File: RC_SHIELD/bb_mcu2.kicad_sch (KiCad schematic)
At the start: 14 parts, among them J26 SWD, J27 P3a, SW1 SW_Push, U25 STM32F030K6Tx, Y1 8MHz

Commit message: footprints assigned
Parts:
- C10, C11, C12, C13, C14, C15, C16, C9: footprint (none) -> Capacitor_SMD:C_0805_2012Metric_Pad1.18x1.45mm_HandSolder
- J26: footprint (none) -> Connector_PinHeader_2.54mm:PinHeader_1x05_P2.54mm_Vertical_SMD_Pin1Left
- J27: footprint (none) -> Connector_Dsub:DSUB-37_Female_Horizontal_P2.77x2.84mm_EdgePinOffset7.70mm_Housed_MountingHolesOffset9.12mm
- R35: footprint (none) -> Resistor_SMD:R_0805_2012Metric_Pad1.20x1.40mm_HandSolder
- SW1: footprint (none) -> Button_Switch_SMD:SW_Tactile_SPST_NO_Straight_CK_PTS636Sx25SMTRLFS
- Y1: footprint (none) -> Crystal:Crystal_SMD_3225-4Pin_3.2x2.5mm_HandSoldering
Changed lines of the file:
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@@
       (effects (font (size 1.27 1.27)))
     )
-    (property "Footprint" "" (at 93.345 32.6898 0)
+    (property "Footprint" "Capacitor_SMD:C_0805_2012Metric_Pad1.18x1.45mm_HandSolder" (at 93.345 32.6898 0)
       (effects (font (size 1.27 1.27)) hide)
     )
@@
       (effects (font (size 1.27 1.27)))
     )
-    (property "Footprint" "" (at 74.295 22.5298 0)
+    (property "Footprint" "Capacitor_SMD:C_0805_2012Metric_Pad1.18x1.45mm_HandSolder" (at 74.295 22.5298 0)
       (effects (font (size 1.27 1.27)) hide)
     )
@@
       (effects (font (size 1.27 1.27)))
     )
-    (property "Footprint" "" (at 29.845 47.2948 0)
+    (property "Footprint" "Capacitor_SMD:C_0805_2012Metric_Pad1.18x1.45mm_HandSolder" (at 29.845 47.2948 0)
       (effects (font (size 1.27 1.27)) hide)
     )
@@
       (effects (font (size 1.27 1.27)))
     )
-    (property "Footprint" "" (at 35.56 53.975 0)
+    (property "Footprint" "Crystal:Crystal_SMD_3225-4Pin_3.2x2.5mm_HandSoldering" (at 35.56 53.975 0)
       (effects (font (size 1.27 1.27)) hide)
     )
@@
       (effects (font (size 1.27 1.27)))
     )
-    (property "Footprint" "" (at 74.295 32.6898 0)
+    (property "Footprint" "Capacitor_SMD:C_0805_2012Metric_Pad1.18x1.45mm_HandSolder" (at 74.295 32.6898 0)
       (effects (font (size 1.27 1.27)) hide)
     )
@@
       (effects (font (size 1.27 1.27)))
     )
-    (property "Footprint" "" (at 47.625 33.9598 0)
+    (property "Footprint" "Capacitor_SMD:C_0805_2012Metric_Pad1.18x1.45mm_HandSolder" (at 47.625 33.9598 0)
       (effects (font (size 1.27 1.27)) hide)
     )
@@
       (effects (font (size 1.27 1.27)))
     )
-    (property "Footprint" "" (at 93.345 22.5298 0)
+    (property "Footprint" "Capacitor_SMD:C_0805_2012Metric_Pad1.18x1.45mm_HandSolder" (at 93.345 22.5298 0)
       (effects (font (size 1.27 1.27)) hide)
     )
@@
       (effects (font (size 1.27 1.27)) (justify left))
     )
-    (property "Footprint" "" (at 56.2102 30.48 0)
+    (property "Footprint" "Capacitor_SMD:C_0805_2012Metric_Pad1.18x1.45mm_HandSolder" (at 56.2102 30.48 0)
       (effects (font (size 1.27 1.27)) hide)
     )
@@
       (effects (font (size 1.27 1.27)))
     )
-    (property "Footprint" "" (at 29.845 58.7248 0)
+    (property "Footprint" "Capacitor_SMD:C_0805_2012Metric_Pad1.18x1.45mm_HandSolder" (at 29.845 58.7248 0)
       (effects (font (size 1.27 1.27)) hide)
     )
@@
       (effects (font (size 1.27 1.27)))
     )
-    (property "Footprint" "" (at 43.815 21.59 0)
+    (property "Footprint" "Button_Switch_SMD:SW_Tactile_SPST_NO_Straight_CK_PTS636Sx25SMTRLFS" (at 43.815 21.59 0)
       (effects (font (size 1.27 1.27)) hide)
     )
@@
       (effects (font (size 1.27 1.27)) (justify left))
     )
-    (property "Footprint" "" (at 254 80.01 0)
+    (property "Footprint" "Connector_Dsub:DSUB-37_Female_Horizontal_P2.77x2.84mm_EdgePinOffset7.70mm_Housed_MountingHolesOffset9.12mm" (at 254 80.01 0)
       (effects (font (size 1.27 1.27)) hide)
     )
@@
       (effects (font (size 1.27 1.27)))
     )
-    (property "Footprint" "" (at 48.26 61.468 90)
+    (property "Footprint" "Resistor_SMD:R_0805_2012Metric_Pad1.20x1.40mm_HandSolder" (at 48.26 61.468 90)
       (effects (font (size 1.27 1.27)) hide)
     )
@@
       (effects (font (size 1.27 1.27)) (justify left))
     )
-    (property "Footprint" "" (at 139.065 85.09 0)
-      (effects (font (size 1.27 1.27)) hide)
-    )
+    (property "Footprint" "Connector_PinHeader_2.54mm:PinHeader_1x05_P2.54mm_Vertical_SMD_Pin1Left" (at 139.065 85.09 0)
+      (effects (font (size 1.27 1.27)) hide)
+    )

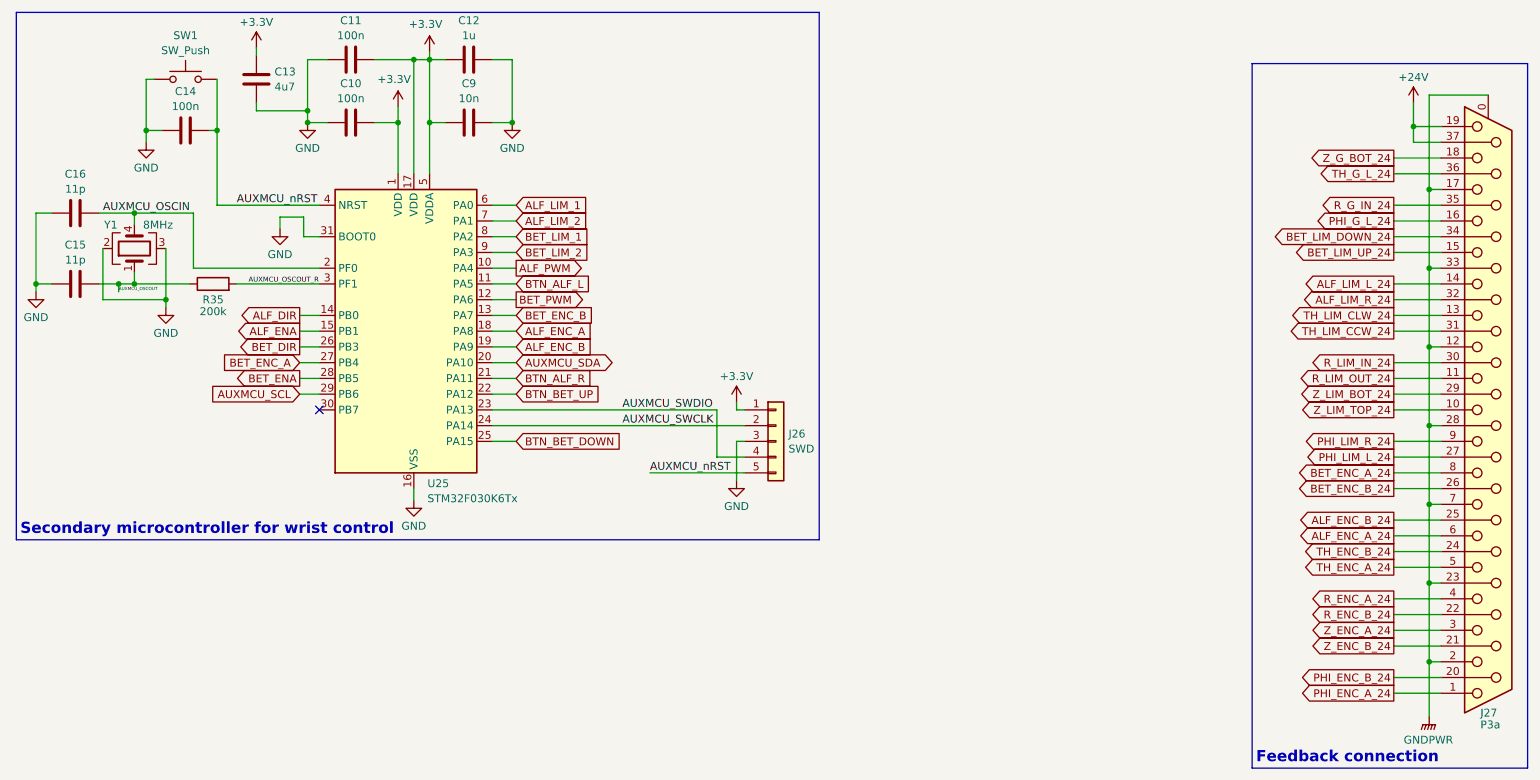
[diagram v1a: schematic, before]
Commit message: Fixed typos and names in schematic, changed optocoupler resistors; added .gitgnore file
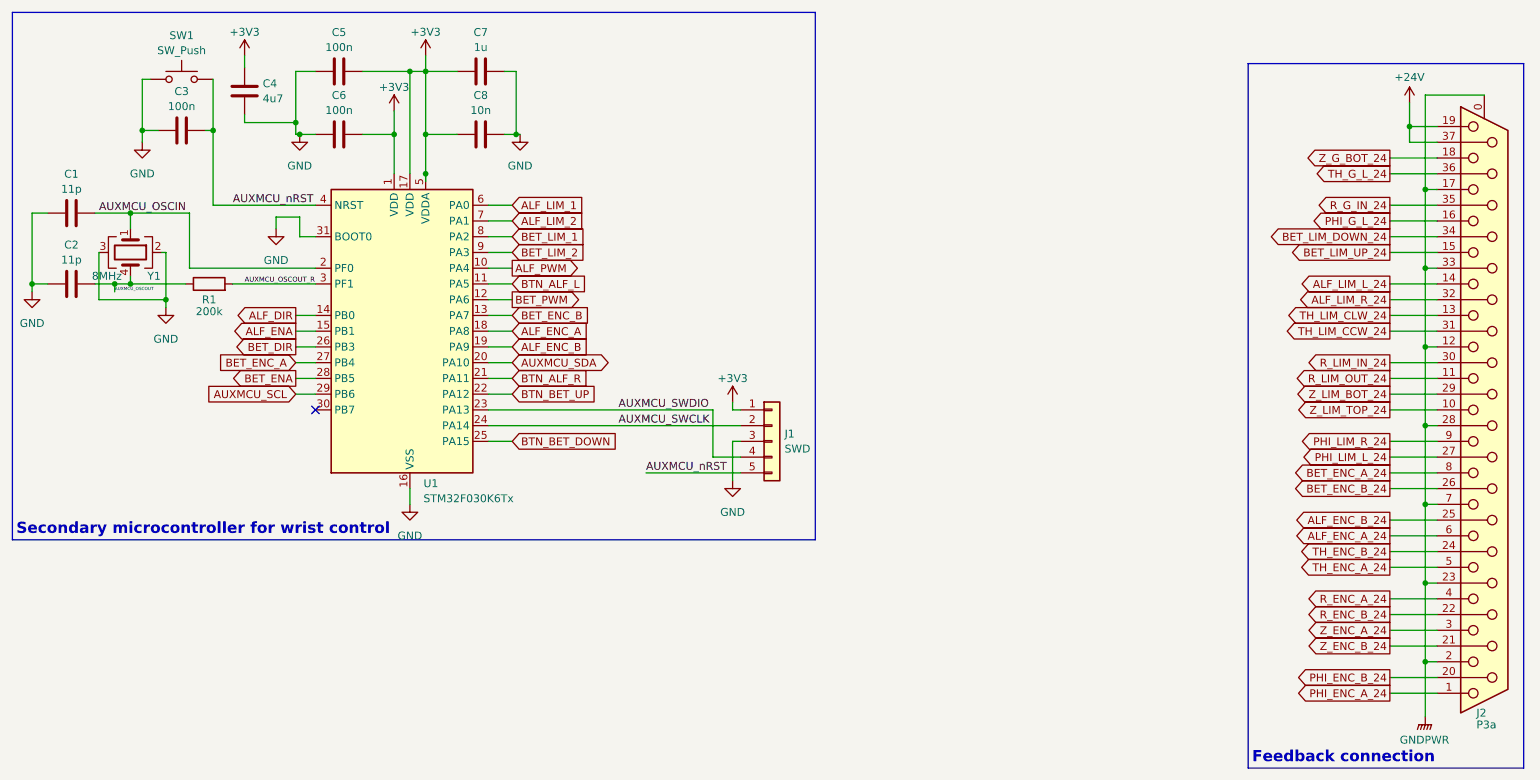
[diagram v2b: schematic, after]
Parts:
- J1: renamed from J26; footprint Connector_PinHeader_2.54mm:PinHeader_1x05_P2.54mm_Vertical_SMD_Pin1Left -> Connector_PinHeader_2.54mm:PinHeader_1x05_P2.54mm_Vertical
- renumbered C16 to C1, C15 to C2, C14 to C3, C13 to C4, C11 to C5, C10 to C6, C12 to C7, C9 to C8, J27 to J2, R35 to R1, U25 to U1
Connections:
- net AUXMCU_OSCIN: now also Y1.1; no longer Y1.4
- net AUXMCU_OSCOUT: now also Y1.4; no longer Y1.1
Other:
- moved on the sheet: C1, C2, C3, C4, C5, C6, C7, C8, J1, J2, R1, SW1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

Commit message: [SCH] added "exclude from BOM" signs
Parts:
- U1: now left out of the parts list
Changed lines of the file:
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@@
   )
   (symbol (lib_id "MCU_ST_STM32F0:STM32F030K6Tx") (at 77.47 67.31 0) (unit 1)
-    (in_bom yes) (on_board yes) (dnp no) (fields_autoplaced)
+    (in_bom no) (on_board yes) (dnp no) (fields_autoplaced)
     (property "Reference" "U1" (at 82.2041 91.8901 0)
       (effects (font (size 1.27 1.27)) (justify left))

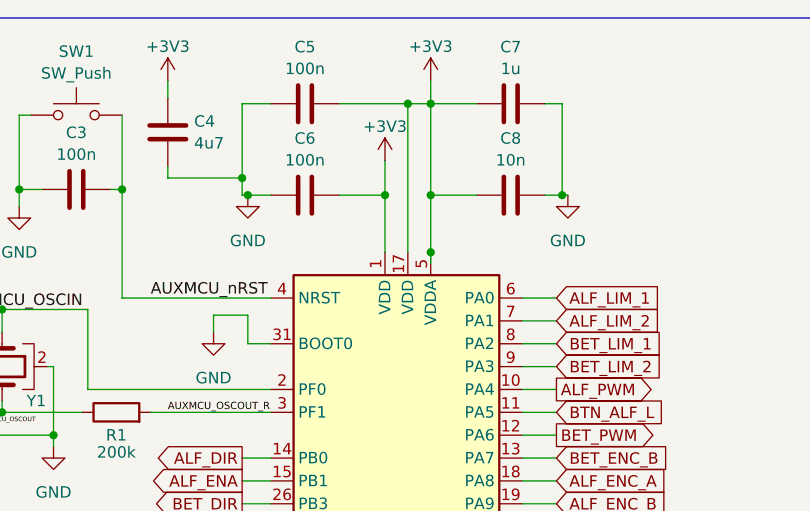
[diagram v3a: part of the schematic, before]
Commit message: [SCH] fixed Nucleo papercuts
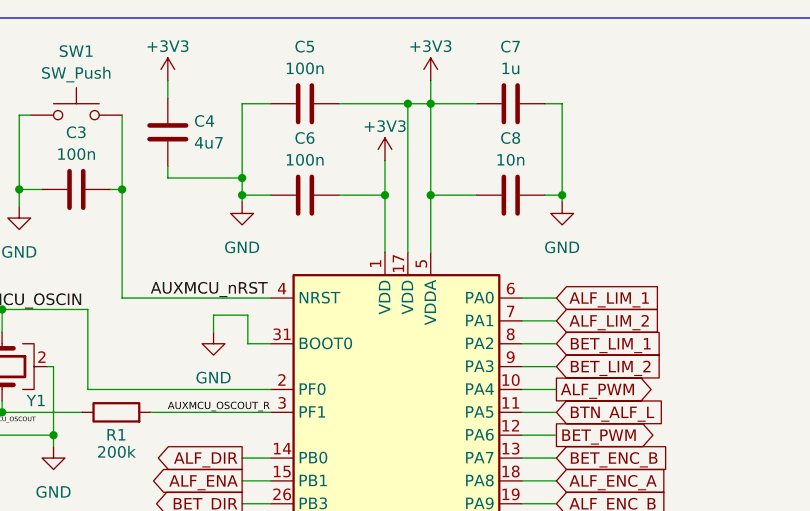
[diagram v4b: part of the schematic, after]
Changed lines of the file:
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@@
   (junction (at 243.84 44.45) (diameter 0) (color 0 0 0 0)
   )
-  (junction (at 62.23 35.56) (diameter 0) (color 0 0 0 0)
-  )
   (junction (at 243.84 120.65) (diameter 0) (color 0 0 0 0)
   )
@@
   (junction (at 243.84 57.15) (diameter 0) (color 0 0 0 0)
   )
+  (junction (at 61.595 35.56) (diameter 0) (color 0 0 0 0)
+  )
   (junction (at 243.84 82.55) (diameter 0) (color 0 0 0 0)
   )
@@
   )
   (junction (at 32.385 59.69) (diameter 0) (color 0 0 0 0)
-  )
-  (junction (at 82.55 41.91) (diameter 0) (color 0 0 0 0)
   )
   (no_connect (at 64.77 80.01))
@@
     (stroke (width 0) (type default))
   )
+  (wire (pts (xy 61.595 35.56) (xy 64.77 35.56))
+    (stroke (width 0) (type default))
+  )
   (wire (pts (xy 92.71 57.15) (xy 96.52 57.15))
     (stroke (width 0) (type default))
@@
     (stroke (width 0) (type default))
   )
-  (wire (pts (xy 61.595 35.56) (xy 62.23 35.56))
-    (stroke (width 0) (type default))
-  )
   (wire (pts (xy 61.595 72.39) (xy 64.77 72.39))
     (stroke (width 0) (type default))
@@
     (stroke (width 0) (type default))
   )
-  (wire (pts (xy 97.155 35.56) (xy 97.79 35.56))
-    (stroke (width 0) (type default))
-  )
   (wire (pts (xy 92.71 85.09) (xy 96.52 85.09))
     (stroke (width 0) (type default))
   )
-  (wire (pts (xy 82.55 43.18) (xy 82.55 41.91))
-    (stroke (width 0) (type default))
-  )
   (wire (pts (xy 51.435 59.69) (xy 64.77 59.69))
     (stroke (width 0) (type default))
@@
     (stroke (width 0) (type default))
   )
+  (wire (pts (xy 61.595 36.322) (xy 61.595 35.56))
+    (stroke (width 0) (type default))
+  )
   (wire (pts (xy 53.34 33.655) (xy 61.595 33.655))
     (stroke (width 0) (type default))
@@
     (stroke (width 0) (type default))
   )
+  (wire (pts (xy 97.155 36.322) (xy 97.155 35.56))
+    (stroke (width 0) (type default))
+  )
   (wire (pts (xy 238.125 67.31) (xy 245.745 67.31))
     (stroke (width 0) (type default))
@@
   )
   (wire (pts (xy 92.71 69.85) (xy 96.52 69.85))
-    (stroke (width 0) (type default))
-  )
-  (wire (pts (xy 62.23 35.56) (xy 64.77 35.56))
     (stroke (width 0) (type default))
   )
@@
     )
   )
-  (symbol (lib_id "power:GND") (at 97.79 35.56 0) (unit 1)
-    (in_bom yes) (on_board yes) (dnp no) (fields_autoplaced)
-    (property "Reference" "#PWR012" (at 97.79 41.91 0)
-      (effects (font (size 1.27 1.27)) hide)
-    )
-    (property "Value" "GND" (at 97.79 40.64 0)
-      (effects (font (size 1.27 1.27)))
-    )
-    (property "Footprint" "" (at 97.79 35.56 0)
-      (effects (font (size 1.27 1.27)) hide)
-    )
-    (property "Datasheet" "" (at 97.79 35.56 0)
+  (symbol (lib_id "power:GND") (at 97.155 36.322 0) (unit 1)
+    (in_bom yes) (on_board yes) (dnp no) (fields_autoplaced)
+    (property "Reference" "#PWR012" (at 97.155 42.672 0)
+      (effects (font (size 1.27 1.27)) hide)
+    )
+    (property "Value" "GND" (at 97.155 41.402 0)
+      (effects (font (size 1.27 1.27)))
+    )
+    (property "Footprint" "" (at 97.155 36.322 0)
+      (effects (font (size 1.27 1.27)) hide)
+    )
+    (property "Datasheet" "" (at 97.155 36.322 0)
       (effects (font (size 1.27 1.27)) hide)
     )
@@
     )
   )
-  (symbol (lib_id "power:GND") (at 62.23 35.56 0) (unit 1)
-    (in_bom yes) (on_board yes) (dnp no) (fields_autoplaced)
-    (property "Reference" "#PWR016" (at 62.23 41.91 0)
-      (effects (font (size 1.27 1.27)) hide)
-    )
-    (property "Value" "GND" (at 62.23 40.64 0)
-      (effects (font (size 1.27 1.27)))
-    )
-    (property "Footprint" "" (at 62.23 35.56 0)
-      (effects (font (size 1.27 1.27)) hide)
-    )
-    (property "Datasheet" "" (at 62.23 35.56 0)
-      (effects (font (size 1.27 1.27)) hide)
-    )
+  (symbol (lib_id "power:GND") (at 61.595 36.322 0) (unit 1)
+    (in_bom yes) (on_board yes) (dnp no) (fields_autoplaced)
+    (property "Reference" "#PWR016" (at 61.595 42.672 0)
+      (effects (font (size 1.27 1.27)) hide)
+    )
+    (property "Value" "GND" (at 61.595 41.402 0)
+      (effects (font (size 1.27 1.27)))
+    )
+    (property "Footprint" "" (at 61.595 36.322 0)
+      (effects (font (size 1.27 1.27)) hide)
+    )
+    (property "Datasheet" "" (at 61.595 36.322 0)
+      (effects (font (size 1.27 1.27)) hide)
+    )
